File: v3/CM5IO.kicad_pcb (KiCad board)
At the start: 4 copper layers, 72 x 58 mm, 42 parts, among them J1 USB_C_Receptacle_USB2.0, J2 Conn_01x22_Female, J3 Conn_01x22_Female, J4 Conn_01x02, J5 UART Connection, J6 Micro_SD_Card_Det, Q1 AO3400A, SW1 Right angle Tact button, SW2 Right angle Tact button, U1 74LVC1G07SE-7, U2 ASM330LHHTR, U3 XIAO_RM3100_Breakout, U4 RT9742GGJ5, U5 LSM9DS1

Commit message: Various pcb mods
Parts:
- removed Module1: ComputeModule5-CM5, CM5IO:Raspberry-Pi-5-Compute-Module
- added J8: 10164227-1001A1RLF, CM5IO:CM5_connector, B.Cu at (176.1, 76.4)
- added J9: 10164227-1001A1RLF, CM5IO:CM5_connector, B.Cu at (142.1, 76.4)
- added U6: ~, CM5IO:Raspberry-Pi-5-Compute-Module, B.Cu at (142.2, 76.4)
- J1: value USB_C_Receptacle_USB2.0 -> TYPE-C-31-M-12; footprint Connector_USB:USB_C_Receptacle_GCT_USB4105-xx-A_16P_TopMnt_Horizontal -> CM5IO:HRO_TYPE-C-31-M-12
- LS1: value AST1240MLTRQ -> KMTG1203
- moved J1 1.61 mm to (188.4, 114.6)
- renumbered C5 to C10, C6 to C11, C11 to C3, C10 to C4, C9 to C5, C8 to C6, C3 to C8, C4 to C9, J4 to J5, J5 to J6, J6 to J7, U5 to U1, U1 to U2, U2 to U3, U3 to U4, U4 to U5
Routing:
- net GND: track 419.9 -> 425.4 mm, vias 66 -> 63
- net /USB2_P: track 18.1 -> 20.0 mm
- net /+5v: track 130.2 -> 131.3 mm
- net /USB2_N: track 19.1 -> 19.9 mm

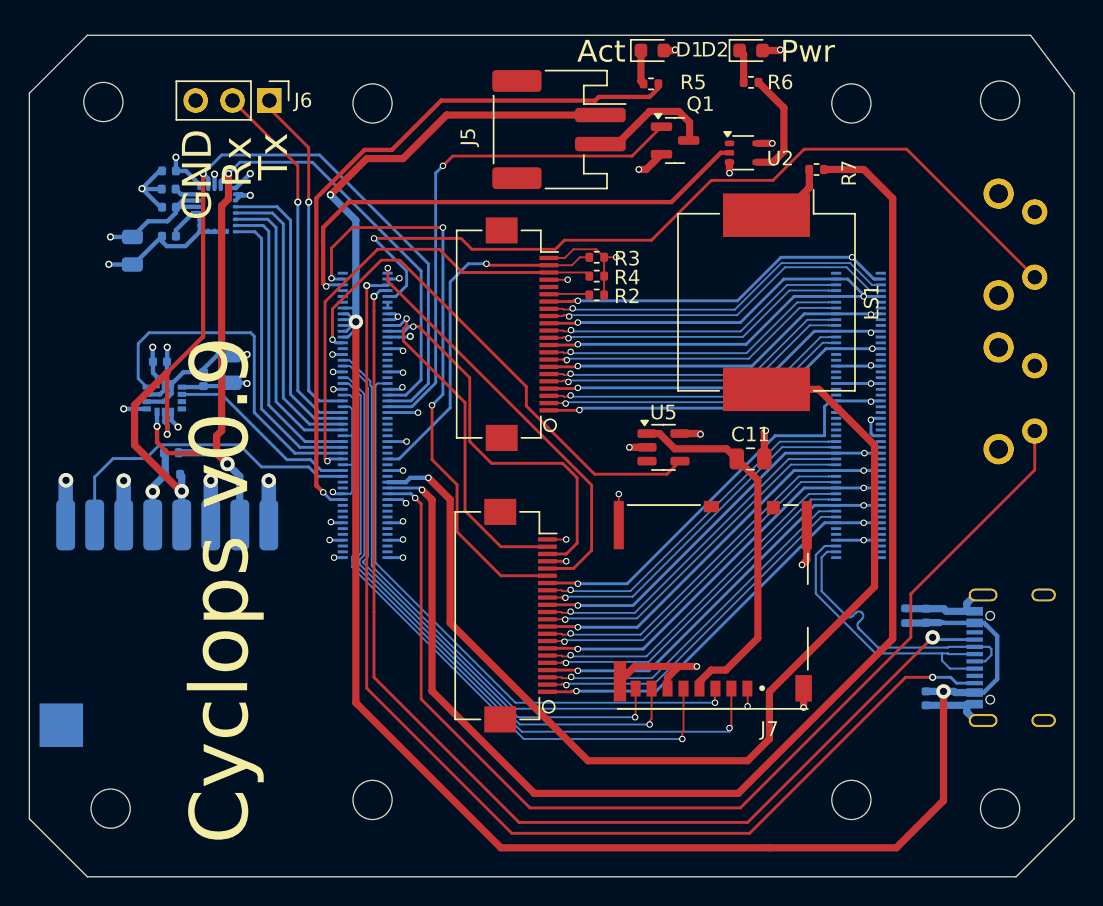
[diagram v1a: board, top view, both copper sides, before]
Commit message: convert to CS20 TOF
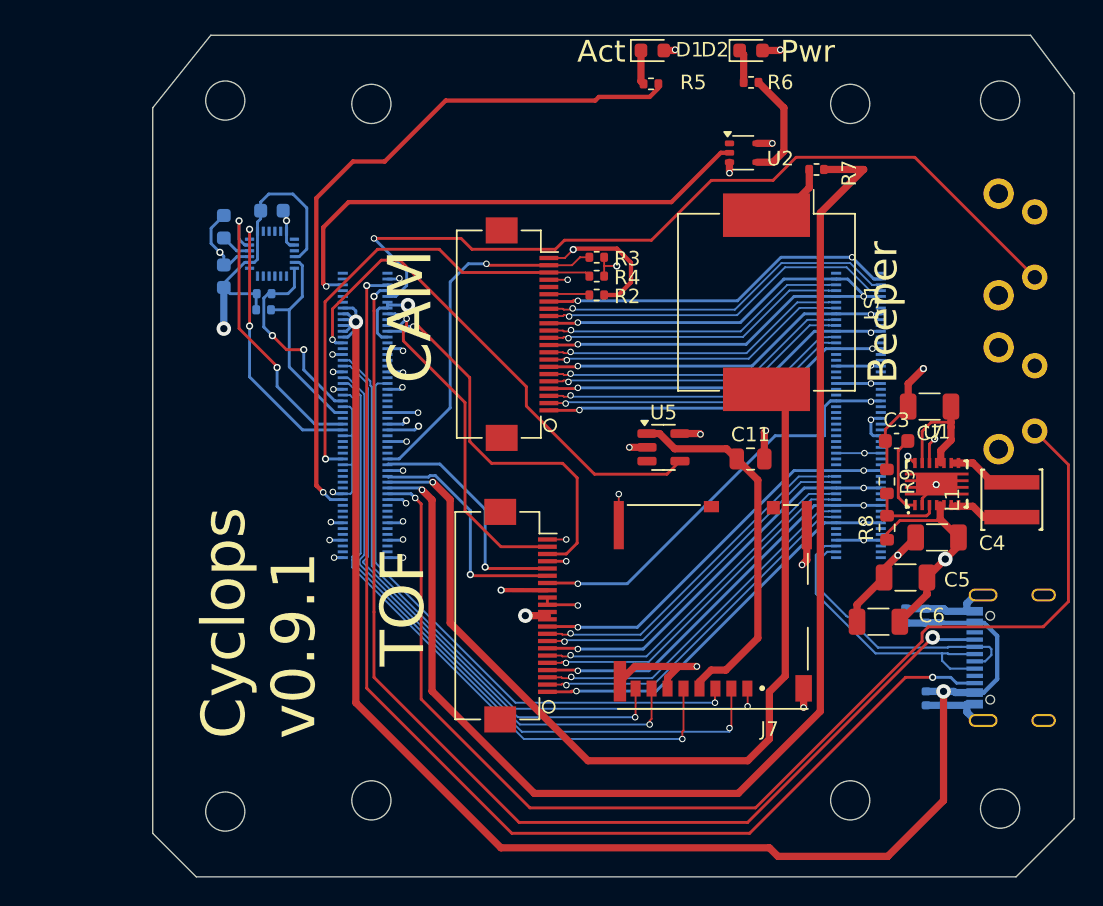
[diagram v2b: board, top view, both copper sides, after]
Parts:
- removed J5: Conn_01x02, Connector_JST:JST_PH_S2B-PH-SM4-TB_1x02-1MP_P2.00mm_Horizontal
- removed J6: UART Connection, Connector_PinHeader_2.54mm:PinHeader_1x03_P2.54mm_Vertical
- removed Q1: AO3400A, Package_TO_SOT_SMD:SOT-23
- removed U4: XIAO_RM3100_Breakout, CM5IO:RM3100_Breakout
- added L1: XFL4020-152MEC, footprint:IND-SMD_L4.0-W4.0-A, F.Cu at (186.2, 103.7)
- added R10: 2.2K 1%, Resistor_SMD:R_0402_1005Metric, B.Cu at (134.6, 90.6)
- added R11: 2.2K 1%, Resistor_SMD:R_0402_1005Metric, B.Cu at (134.7, 89.5)
- C10: value 10u -> 100nF; footprint Capacitor_SMD:C_0805_2012Metric -> Capacitor_SMD:C_0603_1608Metric
- C3: value 10n -> 100nF; footprint Capacitor_SMD:C_0402_1005Metric -> Capacitor_SMD:C_0603_1608Metric; moved to F.Cu
- C4, C5, C7: value 100n -> 22uF; footprint Capacitor_SMD:C_0402_1005Metric -> Capacitor_SMD:C_1206_3216Metric; moved to F.Cu
- C6: value 10u -> 22uF; footprint Capacitor_SMD:C_0805_2012Metric -> Capacitor_SMD:C_1206_3216Metric; moved to F.Cu
- C8, C9: value 100n -> 100nF; footprint Capacitor_SMD:C_0402_1005Metric -> Capacitor_SMD:C_0603_1608Metric
- R8: value 2.2K 1% -> 1M; footprint Resistor_SMD:R_0402_1005Metric -> Resistor_SMD:R_0603_1608Metric; moved to F.Cu
- R9: value 2.2K 1% -> 180k; footprint Resistor_SMD:R_0402_1005Metric -> Resistor_SMD:R_0603_1608Metric; moved to F.Cu
- U1: value LSM9DS1 -> TPS63020DSJR; footprint Package_LGA:LGA-24L_3x3.5mm_P0.43mm -> footprint:VSON-14_L4.0-W3.0-P0.50-BL-EP_TI_DSJ; moved to F.Cu
- U3: value ASM330LHHTR -> ICM-20948; footprint CM5IO:ASM330LHHTR -> CM5IO:QFN40P300X300X105-24N
- moved C4 58.1 mm to (181.1, 106.3)
- moved C5 58.0 mm to (178.9, 109.1)
- moved C6 57.4 mm to (177.0, 112.1), turned to 180 degrees
- moved C7 54.2 mm to (180.5, 97.3)
- moved U1 53.0 mm to (181.0, 102.6), turned to 0 degrees
- moved C3 52.1 mm to (178.3, 99.7), turned to 0 degrees
- moved R8 49.6 mm to (177.6, 105.6), turned to 90 degrees
- moved R9 49.2 mm to (177.6, 102.5), turned to -90 degrees
- moved U3 12.4 mm to (135.2, 86.8), turned to 90 degrees
- moved C10 11.3 mm to (135.2, 83.8), turned to 0 degrees
- moved C8 10.6 mm to (131.9, 84.9)
- moved H1 8.40 mm to (132.0, 76.2)
- moved H2 7.90 mm to (132.0, 125.2)
- moved C9 7.36 mm to (131.9, 88.3), turned to 90 degrees
- moved U6 0.09 mm to (142.1, 76.4)
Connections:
- C10 pad 1: /+3.3v -> /+1.8v
- C3 pad 1: Net-(U1-CAP) -> GND
- C3 pad 2: GND -> Net-(U1-VINA)
- C4 pad 1: Net-(U1-C1) -> +3.3vLED
- C5 pad 1: /+3.3v -> +3.3vLED
- C6 pad 1: /+3.3v -> +3.3vLED
- C7 pad 1: /+3.3v -> +5V
- C8 pad 1: /+3.3v -> Net-(U3-REGOUT)
- C9 pad 1: /+3.3v -> /+1.8v
- J2 pad 11: /CM5_HighSpeed/DPHY0_D2_N -> +3.3vLED
- J2 pad 12: /CM5_HighSpeed/DPHY0_D2_P -> +3.3vLED
- J2 pad 14: /CM5_HighSpeed/DPHY0_D3_N -> GND
- J2 pad 15: /CM5_HighSpeed/DPHY0_D3_P -> /+1.8v
- J2 pad 17: /CM5_GPIO ( Ethernet, GPIO, SDCARD)/CAM_GPIO0 -> /CM5_GPIO ( Ethernet, GPIO, SDCARD)/GPIO6
- J2 pad 18: /CM5_GPIO ( Ethernet, GPIO, SDCARD)/CAM_GPIO1 -> /CM5_GPIO ( Ethernet, GPIO, SDCARD)/GPIO5
- J9 pad 46: /CM5_GPIO ( Ethernet, GPIO, SDCARD)/GPIO22 -> /CM5_GPIO ( Ethernet, GPIO, SDCARD)/EN
- J9 pad 78: /+3.3v -> /+1.8v
- J9 pad 88: /CM5_GPIO ( Ethernet, GPIO, SDCARD)/+1.8v -> /+1.8v
- J9 pad 90: /CM5_GPIO ( Ethernet, GPIO, SDCARD)/+1.8v -> /+1.8v
- R3 pad 1: /+3.3v -> /+1.8v
- R4 pad 1: /+3.3v -> /+1.8v
- R8 pad 1: /+3.3v -> +3.3vLED
- R8 pad 2: /CM5_GPIO ( Ethernet, GPIO, SDCARD)/GPIO2 -> Net-(U1-FB)
- R9 pad 1: /+3.3v -> GND
- R9 pad 2: /CM5_GPIO ( Ethernet, GPIO, SDCARD)/GPIO3 -> Net-(U1-FB)
- U1 pad 1: /+3.3v -> Net-(U1-VINA)
- U1 pad 10: /CM5_GPIO ( Ethernet, GPIO, SDCARD)/GPIO23 -> +5V
- U1 pad 11: /CM5_GPIO ( Ethernet, GPIO, SDCARD)/GPIO24 -> +5V
- U1 pad 12: /CM5_GPIO ( Ethernet, GPIO, SDCARD)/GPIO25 -> /CM5_GPIO ( Ethernet, GPIO, SDCARD)/EN
- U1 pad 13: /CM5_GPIO ( Ethernet, GPIO, SDCARD)/GPIO8 -> +5V
- U1 pad 14: GND -> /CM5_GPIO ( Ethernet, GPIO, SDCARD)/GPIO27
- U1 pad 2: /CM5_GPIO ( Ethernet, GPIO, SDCARD)/GPIO3 -> GND
- U1 pad 3: /+3.3v -> Net-(U1-FB)
- U1 pad 4: /CM5_GPIO ( Ethernet, GPIO, SDCARD)/GPIO2 -> +3.3vLED
- U1 pad 5: GND -> +3.3vLED
- U1 pad 6: GND -> Net-(L1-Pad1)
- U1 pad 7: /+3.3v -> Net-(L1-Pad1)
- U1 pad 8: /+3.3v -> Net-(L1-Pad2)
- U1 pad 9: /CM5_GPIO ( Ethernet, GPIO, SDCARD)/GPIO18 -> Net-(L1-Pad2)
- U3 pad 1: /+3.3v -> unconnected-(U3-NC-Pad1)
- U3 pad 10: unconnected-(U3-NC-Pad10) -> Net-(U3-REGOUT)
- U3 pad 11: unconnected-(U3-NC-Pad11) -> /CM5_GPIO ( Ethernet, GPIO, SDCARD)/GPIO23
- U3 pad 12: /+3.3v -> /CM5_GPIO ( Ethernet, GPIO, SDCARD)/GPIO24
- U3 pad 13: /CM5_GPIO ( Ethernet, GPIO, SDCARD)/GPIO3 -> /+1.8v
- U3 pad 14: /CM5_GPIO ( Ethernet, GPIO, SDCARD)/GPIO2 -> unconnected-(U3-NC-Pad14)
- U3 pad 2: GND -> unconnected-(U3-NC-Pad2)
- U3 pad 3: GND -> unconnected-(U3-NC-Pad3)
- U3 pad 4: /CM5_GPIO ( Ethernet, GPIO, SDCARD)/GPIO7 -> unconnected-(U3-NC-Pad4)
- U3 pad 5: /+3.3v -> unconnected-(U3-NC-Pad5)
- U3 pad 6: GND -> unconnected-(U3-NC-Pad6)
- U3 pad 7: GND -> unconnected-(U3-AUX_CL-Pad7)
- U3 pad 8: /+3.3v -> /+1.8v
- U3 pad 9: /CM5_GPIO ( Ethernet, GPIO, SDCARD)/GPIO12 -> GND
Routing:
- net /CM5_GPIO ( Ethernet, GPIO, SDCARD)/EN: track 0.00 -> 86.3 mm, vias 0 -> 2
- net /+1.8v: track 0.00 -> 84.9 mm, vias 0 -> 4
- net /CM5_GPIO ( Ethernet, GPIO, SDCARD)/GPIO27: track 0.00 -> 79.5 mm, vias 0 -> 2
- net /CM5_GPIO ( Ethernet, GPIO, SDCARD)/GPIO3: track 66.5 -> 0.00 mm, vias 3 -> 0
- net /CM5_GPIO ( Ethernet, GPIO, SDCARD)/GPIO2: track 63.6 -> 0.00 mm, vias 3 -> 0
- net +3.3vLED: track 0.00 -> 59.2 mm, vias 0 -> 2
- net /+3.3v: track 50.3 -> 91.4 mm, vias 18 -> 7
- net /CM5_GPIO ( Ethernet, GPIO, SDCARD)/CAM_GPIO0: track 40.6 -> 0.00 mm, vias 3 -> 0
- net GND: track 425.4 -> 387.5 mm, vias 63 -> 59
- net /CM5_GPIO ( Ethernet, GPIO, SDCARD)/GPIO4: track 35.3 -> 0.00 mm, vias 1 -> 0
- net /CM5_GPIO ( Ethernet, GPIO, SDCARD)/CAM_GPIO1: track 29.2 -> 0.00 mm, vias 1 -> 0
- net /+5v: track 131.3 -> 102.7 mm, vias 3 -> 2
- net /CM5_HighSpeed/DPHY0_D2_P: track 24.4 -> 0.00 mm, vias 1 -> 0
- net /CM5_HighSpeed/DPHY0_D2_N: track 24.4 -> 0.00 mm, vias 1 -> 0
- net /CM5_HighSpeed/DPHY0_D3_P: track 24.3 -> 0.00 mm, vias 1 -> 0
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- removed copper zone on In1.Cu, net /+3.3v
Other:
- board size 72 x 58 mm -> 63.5 x 58 mm
- board text added: "Beeper"
- board text added: "CAM"
- board text added: "Cyclops v0.9.1"
- board text added: "MAG"
- board text added: "TOF"
- board text added: "USB"
- board text removed: "Cyclops v0.9"
- board text removed: "GND"
- board text removed: "Rx"
- board text removed: "Tx"
